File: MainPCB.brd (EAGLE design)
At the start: 165.1 x 114.3 mm, 75 parts, among them J2 DCJ0202, J3 FEMALE 2x3, X1 8MHz

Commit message: routing blows
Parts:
- moved C18 121.4 mm to (93.8, 43.5), flipped to the bottom, turned to 270 degrees
- moved C19 111.7 mm to (76.2, 43.5), flipped to the bottom, turned to 270 degrees
- moved C20 110.2 mm to (76.2, 37.4), flipped to the bottom, turned to 90 degrees
- moved C21 106.2 mm to (55.7, 43.7), flipped to the bottom, turned to 270 degrees
- moved C22 102.7 mm to (36.5, 44.8), flipped to the bottom, turned to 270 degrees
- moved C23 100.8 mm to (36.4, 38.7), flipped to the bottom, turned to 90 degrees
- moved R16 97.2 mm to (60.0, 58.0), turned to 90 degrees
- moved R15 92.2 mm to (57.0, 58.0), turned to 90 degrees
- moved C15 89.8 mm to (73.6, 30.2), flipped to the bottom, turned to 270 degrees
- moved R14 87.2 mm to (54.0, 58.0), turned to 90 degrees
- moved R13 81.3 mm to (31.0, 68.0)
- moved C16 79.5 mm to (56.0, 30.3), flipped to the bottom, turned to 270 degrees
- moved C17 78.1 mm to (56.1, 24.3), flipped to the bottom, turned to 90 degrees
- moved R2 21.5 mm to (39.4, 44.7), flipped to the bottom, turned to 90 degrees
- moved R1 20.6 mm to (52.5, 43.7), flipped to the bottom, turned to 90 degrees
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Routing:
- net 3.3V: track 0.00 -> 160.1 mm, vias 0 -> 5
- net +5V: track 0.00 -> 84.2 mm, vias 0 -> 1
- net ROW3: track 0.00 -> 36.6 mm
- net 9V: track 0.00 -> 14.2 mm
- net N$3: track 0.00 -> 11.8 mm
- net ROWOUT_3: track 0.00 -> 7.46 mm
- net ROW1: track 0.00 -> 7.44 mm
- net ROW2: track 0.00 -> 7.34 mm
- net ROWOUT_1: track 0.00 -> 7.26 mm
- net ROWOUT_2: track 0.00 -> 7.20 mm
- net ROW5: track 0.00 -> 6.91 mm
- net ROW4: track 0.00 -> 6.88 mm
- net ROWOUT_5: track 0.00 -> 6.77 mm
- net ROWOUT_4: track 0.00 -> 6.69 mm
- net ROW6: track 0.00 -> 6.09 mm
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
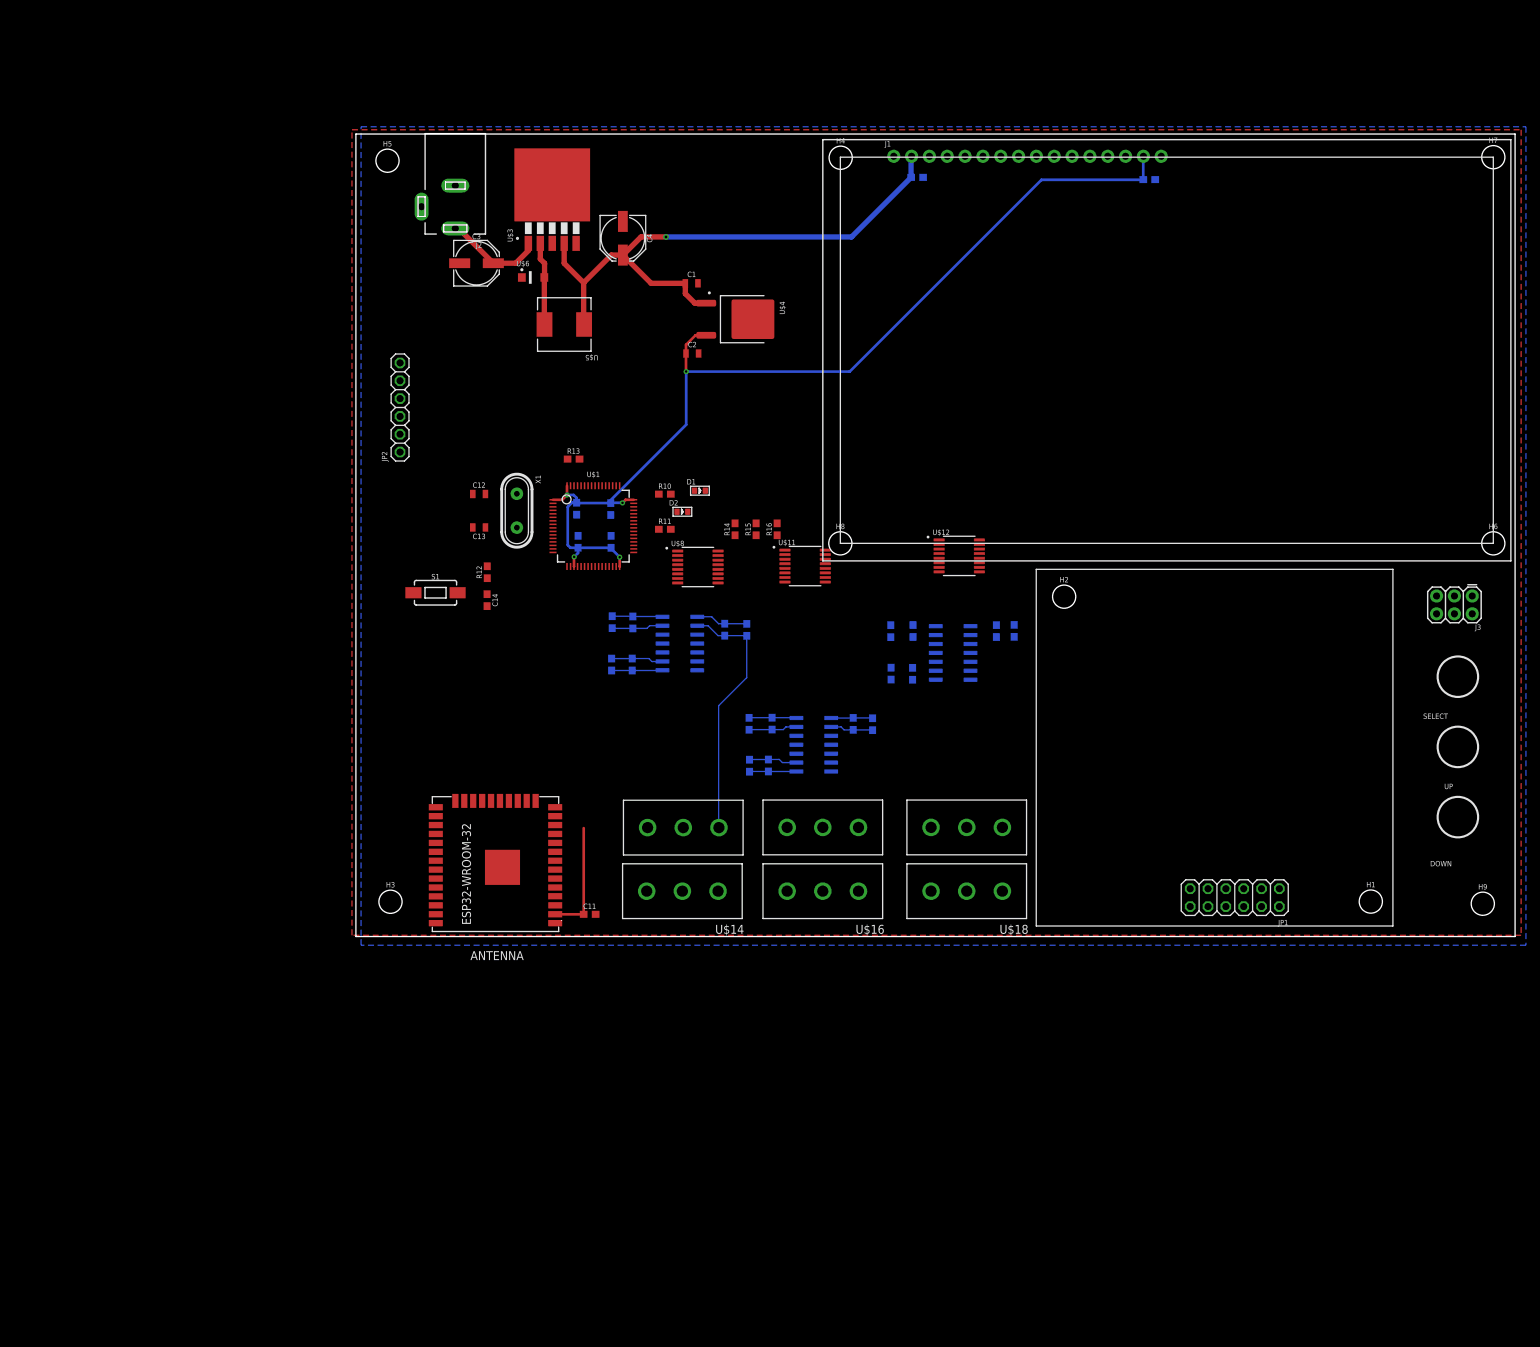
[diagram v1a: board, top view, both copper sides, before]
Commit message: changed layout
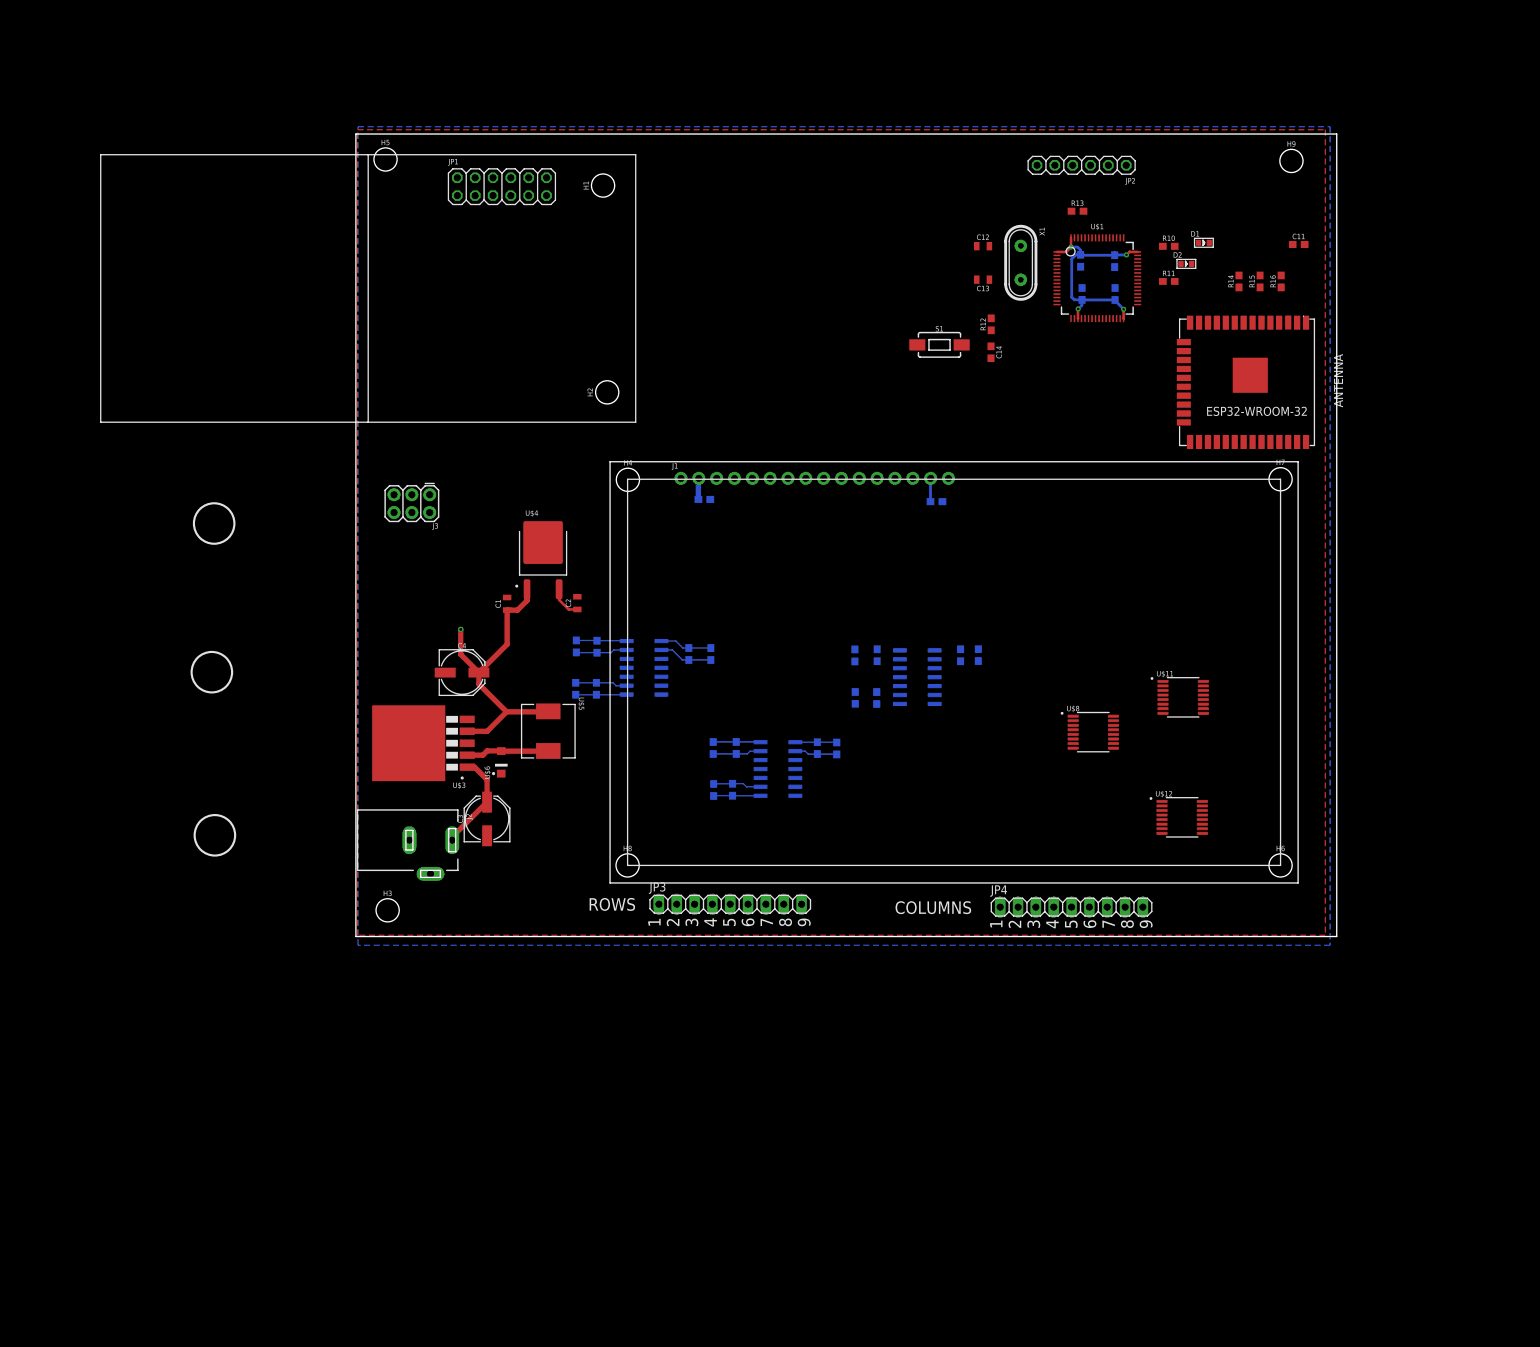
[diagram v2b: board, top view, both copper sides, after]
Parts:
- removed U$13, U$14, U$15, U$16, U$17, U$18: 3PINCONN, SeniorDesignParts:3PINCONN
- added JP3, JP4: (no value), pinhead:1X09
- moved H1 149.5 mm to (35.2, 107.0), turned to 90 degrees
- moved J3 149.2 mm to (10.5, 62.9)
- moved JP1 145.4 mm to (20.8, 106.8), turned to 0 degrees
- moved C11 138.9 mm to (134.3, 98.6)
- moved U$7 131.5 mm to (130.3, 79.8), turned to 270 degrees
- moved H9 109.2 mm to (133.2, 110.5)
- moved JP2 103.0 mm to (103.4, 109.8), turned to 180 degrees
- moved J2 90.3 mm to (10.6, 13.7), turned to 270 degrees
- moved C12 80.0 mm to (89.3, 98.3)
- moved C13 80.0 mm to (89.3, 93.6)
- moved C14 80.0 mm to (90.5, 83.2)
- moved C5 80.0 mm to (108.1, 96.2)
- moved C6 80.0 mm to (103.2, 96.2)
- moved C7 80.0 mm to (103.4, 91.5)
- moved C8 80.0 mm to (108.1, 91.5)
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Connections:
- net COL1: now also JP4.1; no longer U$14.A
- net COL2: now also JP4.2; no longer U$14.B
- net COL3: now also JP4.3; no longer U$14.C
- net COL4: now also JP4.4; no longer U$16.A
- net COL5: now also JP4.5; no longer U$16.B
- net COL6: now also JP4.6; no longer U$16.C
- net COL7: now also JP4.7; no longer U$18.A
- net COL8: now also JP4.8; no longer U$18.B
- net COL9: now also JP4.9; no longer U$18.C
- net ROW1: now also JP3.1; no longer U$13.A
- net ROW2: now also JP3.2; no longer U$13.B
- net ROW3: now also JP3.3; no longer U$13.C
- net ROW4: now also JP3.4; no longer U$15.A
- net ROW5: now also JP3.5; no longer U$15.B
- net ROW6: now also JP3.6; no longer U$15.C
- net ROW7: now also JP3.7; no longer U$17.A
- net ROW8: now also JP3.8; no longer U$17.B
- net ROW9: now also JP3.9; no longer U$17.C
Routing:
- net 3.3V: track 160.1 -> 42.0 mm, vias 5 -> 4
- net +5V: track 84.2 -> 45.8 mm
- net ROW3: track 36.6 -> 7.64 mm
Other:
- board size 165.1 x 114.3 mm -> 139.7 x 114.3 mm
- board text added: "1 2 3 4 5 6 7 8 9"
- board text added: "COLUMNS"
- board text added: "ROWS"
- board text removed: "DOWN"
- board text removed: "SELECT"
- board text removed: "UP"

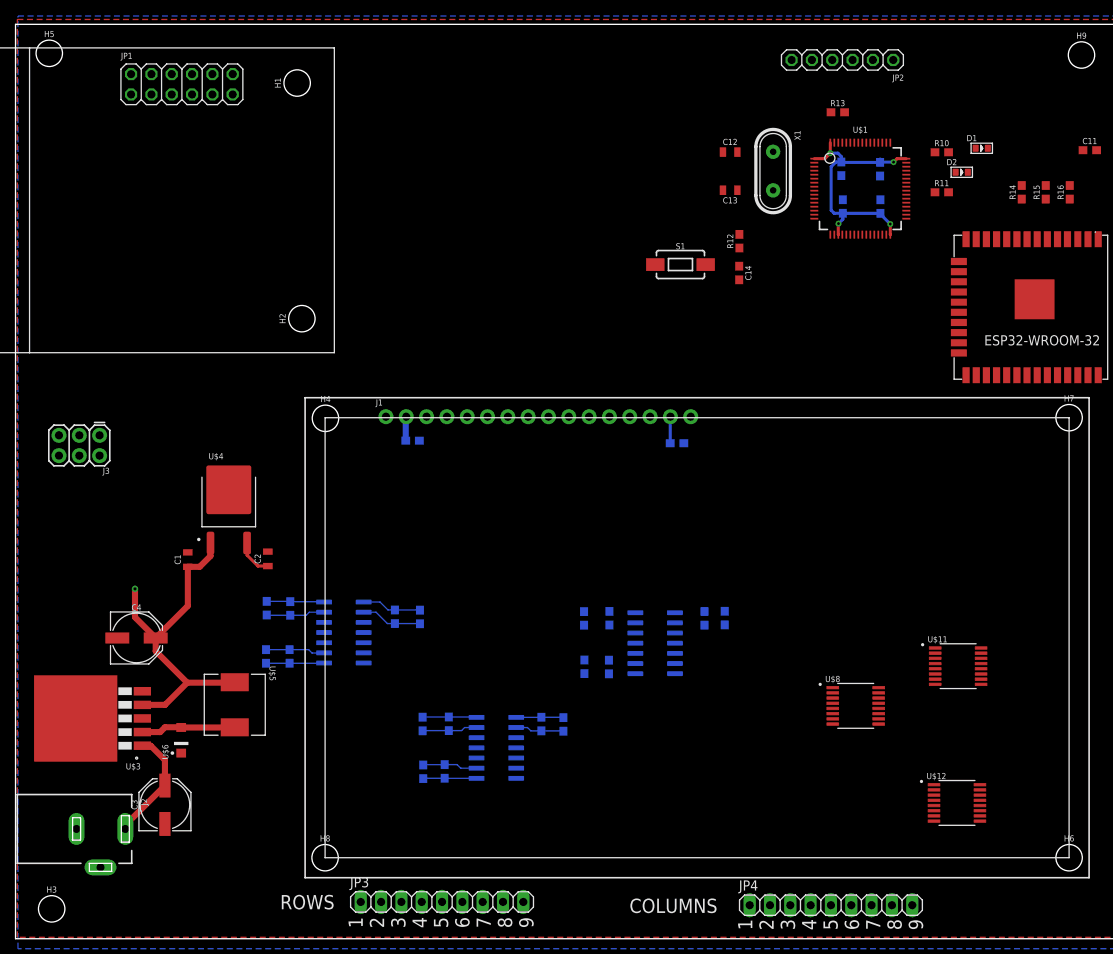
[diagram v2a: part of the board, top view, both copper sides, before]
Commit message: half routed
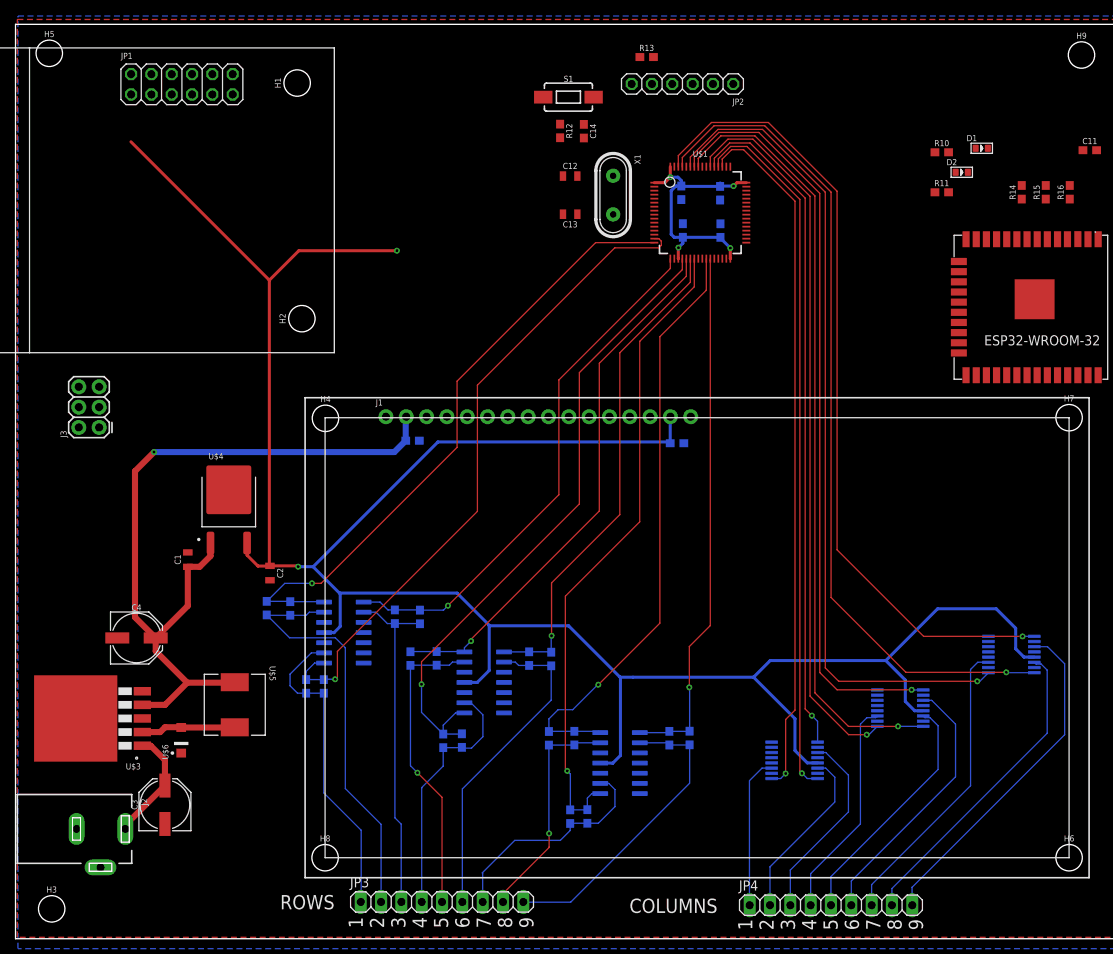
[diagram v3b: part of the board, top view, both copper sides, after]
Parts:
- moved R12 26.3 mm to (68.1, 101.0), turned to 270 degrees
- moved C14 26.3 mm to (71.0, 100.9)
- moved S1 25.2 mm to (69.1, 105.2)
- moved R13 24.9 mm to (78.9, 110.2)
- moved C12 20.2 mm to (69.3, 95.3)
- moved C13 20.2 mm to (69.3, 90.6)
- moved C5 20.2 mm to (88.1, 93.2)
- moved C6 20.2 mm to (83.2, 93.2)
- moved C7 20.2 mm to (83.4, 88.5)
- moved C8 20.2 mm to (88.1, 88.5)
- moved JP2 20.2 mm to (83.4, 106.8)
- moved U$1 20.2 mm to (85.6, 90.8)
- moved X1 20.2 mm to (74.7, 93.0)
- moved U$12 19.8 mm to (124.5, 35.5), flipped to the bottom, turned to 180 degrees
- moved R9 19.3 mm to (69.3, 15.3), turned to 90 degrees
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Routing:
- net 3.3V: track 42.0 -> 332.3 mm, vias 4 -> 6
- net COLOUT_8: track 0.00 -> 104.8 mm, vias 0 -> 1
- net COLOUT_7: track 0.00 -> 103.7 mm, vias 0 -> 1
- net COLOUT_9: track 0.00 -> 100.5 mm, vias 0 -> 1
- net COLOUT_5: track 0.00 -> 97.3 mm, vias 0 -> 1
- net COLOUT_6: track 0.00 -> 95.1 mm, vias 0 -> 1
- net COLOUT_4: track 0.00 -> 90.9 mm, vias 0 -> 1
- net COLOUT_2: track 0.00 -> 88.6 mm, vias 0 -> 1
- net COLOUT_1: track 0.00 -> 87.2 mm, vias 0 -> 1
- net COLOUT_3: track 0.00 -> 84.7 mm, vias 0 -> 1
- net ROWOUT_7: track 0.00 -> 81.3 mm, vias 0 -> 1
- net ROWOUT_1: track 7.26 -> 83.3 mm, vias 0 -> 1
- net ROWOUT_8: track 0.00 -> 74.9 mm, vias 0 -> 1
- net ROWOUT_4: track 6.69 -> 80.8 mm, vias 0 -> 1
- net ROWOUT_2: track 7.20 -> 79.1 mm, vias 0 -> 1
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
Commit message: savey save saved save
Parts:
- added C24, C25, C26: 0.1uF, SparkFun-Capacitors:0603
- added R17: 1k, SparkFun-Resistors:0603
- added R18, R19: 100, SparkFun-Resistors:0603
- added S2, S3: MOMENTARY-SWITCH-SPST-SMD-6.0X3.5MM, SparkFun-Switches:TACTILE_SWITCH_SMD_6.0X3.5MM
- moved J3 83.2 mm to (93.2, 73.1)
- moved R16 46.4 mm to (91.8, 69.7), flipped to the bottom, turned to 0 degrees
- moved R15 45.3 mm to (91.9, 67.1), flipped to the bottom, turned to 0 degrees
- moved R14 44.5 mm to (91.8, 64.5), flipped to the bottom, turned to 0 degrees
- moved R11 11.0 mm to (105.7, 97.9)
- moved D1 10.4 mm to (110.6, 101.0)
- moved U$7 10.4 mm to (132.5, 90.0)
- moved R10 10.4 mm to (105.8, 101.0)
- moved R13 10.1 mm to (79.9, 100.2), flipped to the bottom, turned to 180 degrees
- moved D2 7.97 mm to (110.6, 97.9)
- moved X1 3.89 mm to (71.1, 94.5)
- moved S1 3.76 mm to (69.0, 109.0)
- moved C11 3.68 mm to (137.1, 100.9)
- moved C14 3.60 mm to (72.1, 104.4)
- moved R12 3.58 mm to (69.3, 104.3)
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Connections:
- new net EN: C24.1, C26.1, R17.1, S2.2, U$7.3
- new net IO0: C25.1, S3.2, U$7.25
- new net N$10: R19.2, U$7.34
- new net N$8: R18.2, U$7.35
- net 3.3V: now also R17.2
- net GND: now also C24.2, C25.2, C26.2, S2.1, S3.1
- net RX_ESP: now also R19.1; no longer U$7.34
- net TX_ESP: now also R18.1; no longer U$7.35
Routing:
- net 3.3V: track 332.3 -> 521.0 mm
- net SCLK: track 0.00 -> 98.7 mm, vias 0 -> 3
- net SS: track 0.00 -> 89.9 mm, vias 0 -> 1
- net MOSI: track 0.00 -> 86.7 mm, vias 0 -> 2
- net MISO: track 0.00 -> 66.3 mm
- net TX_ESP: track 0.00 -> 57.4 mm, vias 0 -> 2
- net RX_ESP: track 0.00 -> 52.4 mm, vias 0 -> 2
- net RS: track 0.00 -> 48.5 mm, vias 0 -> 1
- net CSB: track 0.00 -> 39.8 mm, vias 0 -> 1
- net NRST: track 0.00 -> 33.9 mm, vias 0 -> 2
- net BUTT_DOWN: track 0.00 -> 30.1 mm, vias 0 -> 1
- net BUTT_UP: track 0.00 -> 25.4 mm
- net SWDIO: track 0.00 -> 22.4 mm, vias 0 -> 2
- net BUTT_SEL: track 0.00 -> 18.4 mm
- net EN: track 0.00 -> 18.1 mm
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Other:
- board text added: "Main Board v1 ECE477 GRP15 Cynthia Zatlokowicz Mechor De La Garza"
